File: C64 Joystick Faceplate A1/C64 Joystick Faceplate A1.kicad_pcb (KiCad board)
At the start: 2 copper layers, 81.3 x 40.6 mm, 4 parts, among them M1 Mounting, M2 Mounting, M3 Mounting, M4 Mounting

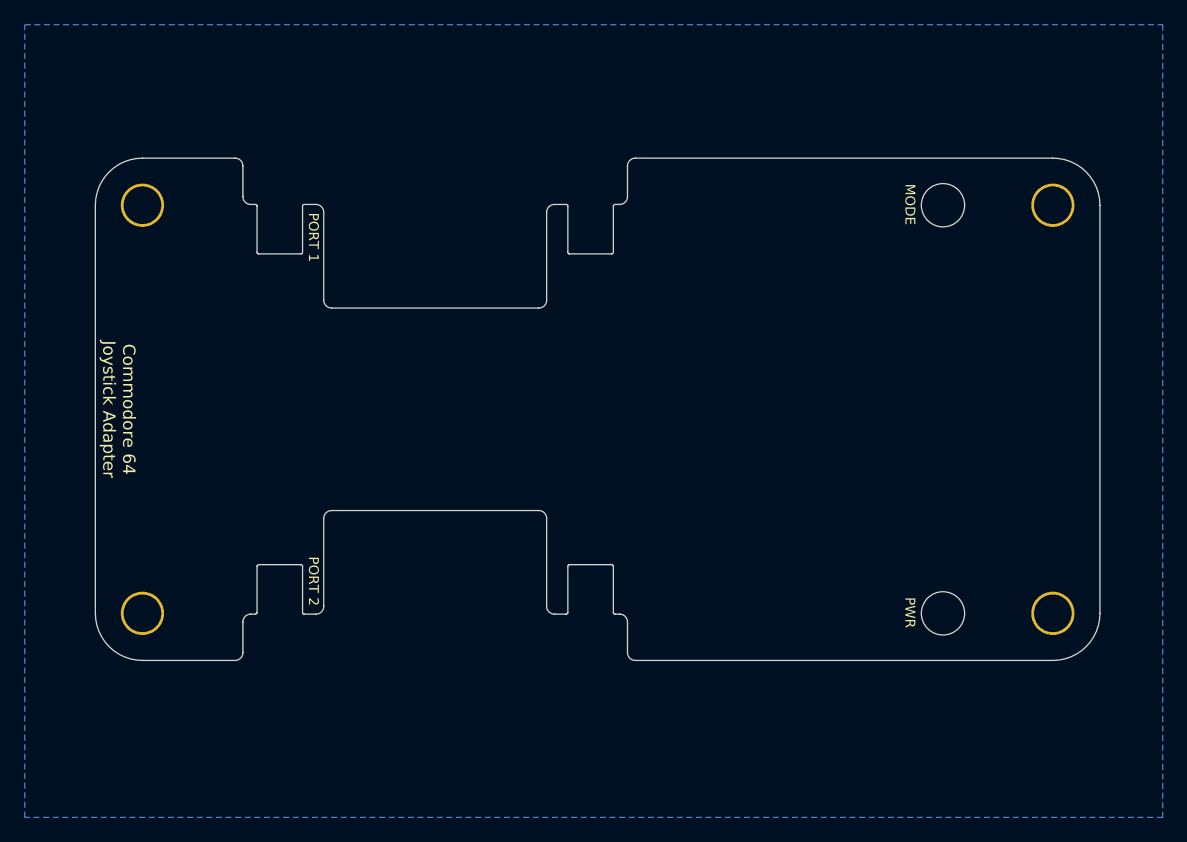
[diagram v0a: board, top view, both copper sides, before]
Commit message: Added faceplate a1
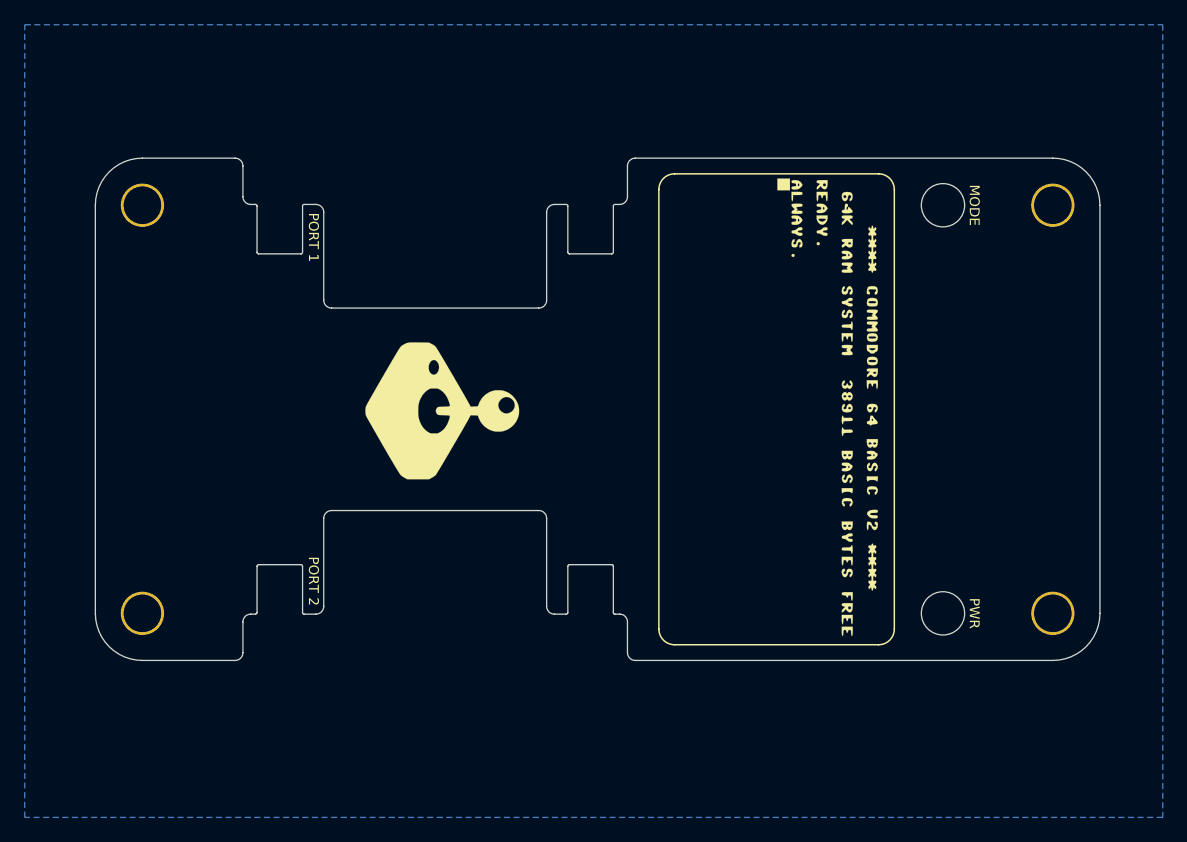
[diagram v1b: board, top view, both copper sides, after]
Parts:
- added G***: LOGO, artwork:joystick_large, B.Cu at (153.7, 92.2)
- added G***: LOGO, artwork:joystick, F.Cu at (124.0, 92.2)
- added G***: LOGO, artwork:boot, F.Cu at (147.6, 92.5)
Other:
- board text removed: "Commodore 64 Joystick Adapter"

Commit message: Changed one faceplate side to gamepad
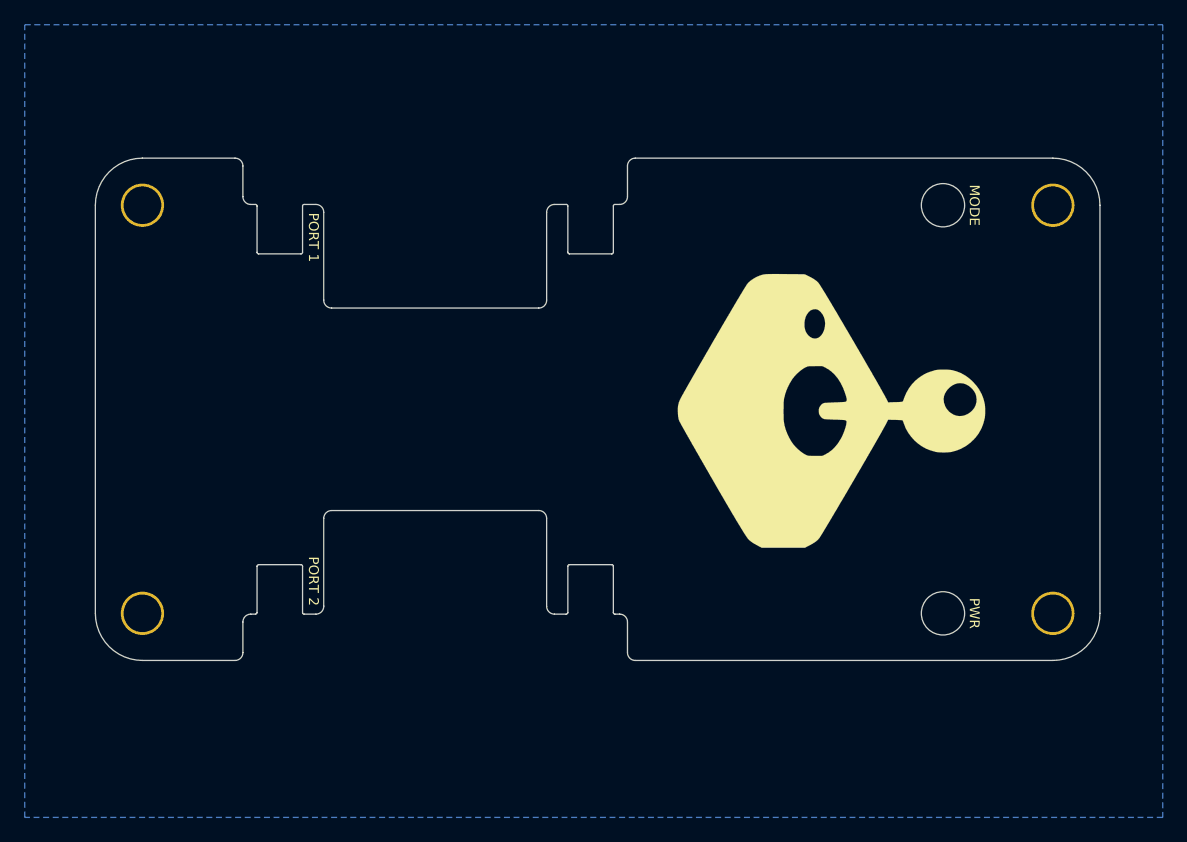
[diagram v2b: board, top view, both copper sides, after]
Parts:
- removed the G*** at (124.0, 92.2)
- removed the G*** at (147.6, 92.5)
- added G***: LOGO, artwork:gamepad_large, B.Cu at (153.7, 92.2)
- G***: moved to F.Cu
- moved G*** 1.78 mm to (155.4, 92.2), turned to 270 degrees

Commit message: Adjusted faceplate cutout to fit better
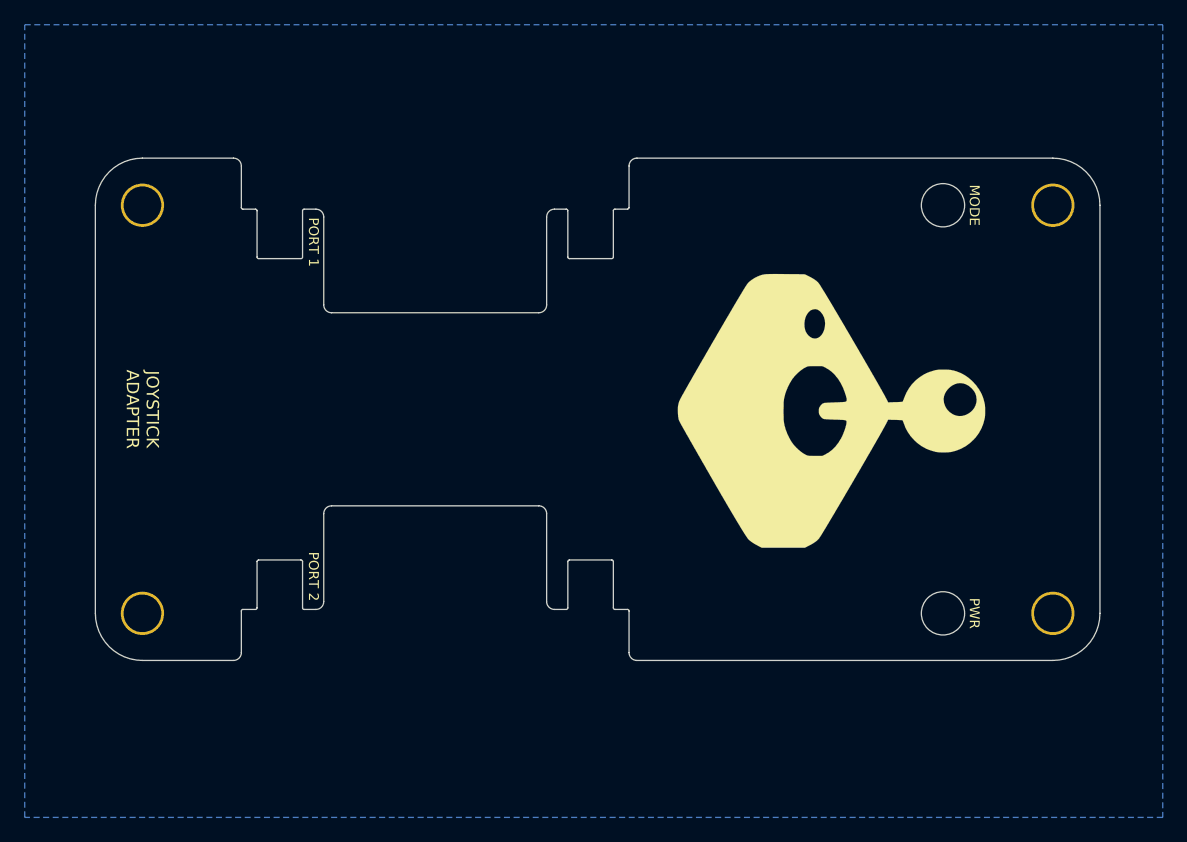
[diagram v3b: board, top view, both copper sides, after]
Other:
- outline, holes or cut-outs redrawn
- board text added: "GAMEPAD ADAPTER"
- board text added: "JOYSTICK ADAPTER"
